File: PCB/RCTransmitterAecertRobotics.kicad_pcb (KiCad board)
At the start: 2 copper layers, 124.5 x 86.4 mm, 36 parts

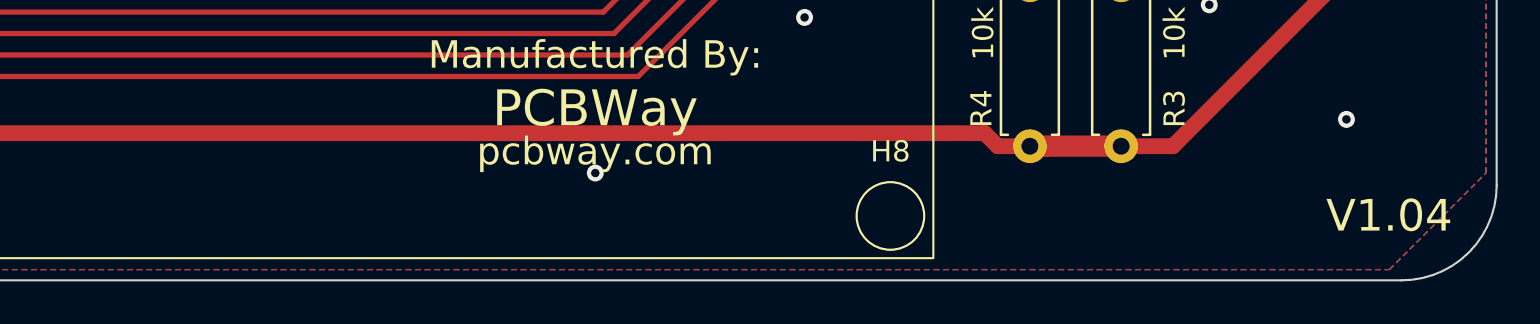
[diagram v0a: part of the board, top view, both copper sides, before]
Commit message: code no longer freezes if gyro doesnt work.
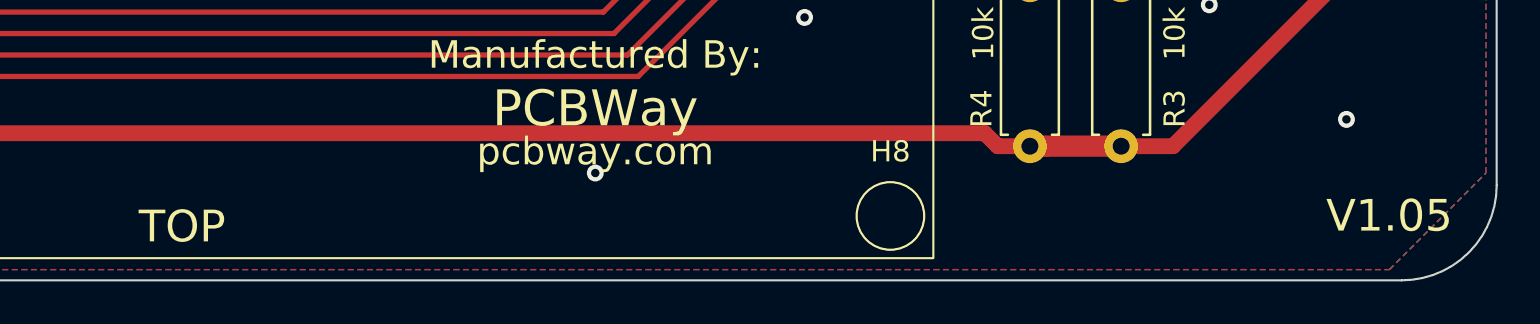
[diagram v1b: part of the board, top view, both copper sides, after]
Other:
- board text added: "BOTTOM"
- board text added: "TOP"
- board text added: "V1.05"
- board text removed: "V1.04"
